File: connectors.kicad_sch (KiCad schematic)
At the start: 5 parts

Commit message: Connect sensors to the MCU
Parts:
- gave numbers to parts that had none: 5
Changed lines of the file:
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@@
 (kicad_sch (version 20211123) (generator eeschema)
   (paper "A4")
+  (title_block
+    (date "2022-12-16")
+    (rev "0.1.0")
+  )
   (wire (pts (xy 219.71 95.25) (xy 220.98 95.25))
     (stroke (width 0) (type default) (color 0 0 0 0))
@@
   (symbol (lib_id "Connector_Generic:Conn_01x03") (at 226.06 97.79 0) (unit 1)
     (in_bom yes) (on_board yes)
-    (property "Reference" "J?" (id 0) (at 227.33 91.4401 0)
+    (property "Reference" "J7" (id 0) (at 227.33 91.4401 0)
       (effects (font (size 1.27 1.27)) (justify right))
     )
@@
   (symbol (lib_id "power:GND") (at 219.71 101.6 0) (unit 1)
     (in_bom yes) (on_board yes) (fields_autoplaced)
-    (property "Reference" "#PWR?" (id 0) (at 219.71 107.95 0)
+    (property "Reference" "#PWR0145" (id 0) (at 219.71 107.95 0)
       (effects (font (size 1.27 1.27)) hide)
     )
@@
   (symbol (lib_id "Connector_Generic:Conn_01x03") (at 190.5 97.79 0) (unit 1)
     (in_bom yes) (on_board yes)
-    (property "Reference" "J?" (id 0) (at 191.77 91.4401 0)
+    (property "Reference" "J6" (id 0) (at 191.77 91.4401 0)
       (effects (font (size 1.27 1.27)) (justify right))
     )
@@
   (symbol (lib_id "power:GND") (at 114.3 101.6 0) (unit 1)
     (in_bom yes) (on_board yes) (fields_autoplaced)
-    (property "Reference" "#PWR?" (id 0) (at 114.3 107.95 0)
+    (property "Reference" "#PWR0143" (id 0) (at 114.3 107.95 0)
       (effects (font (size 1.27 1.27)) hide)
     )
@@
   (symbol (lib_id "power:+3.3V") (at 184.15 93.98 0) (unit 1)
     (in_bom yes) (on_board yes) (fields_autoplaced)
-    (property "Reference" "#PWR?" (id 0) (at 184.15 97.79 0)
+    (property "Reference" "#PWR0146" (id 0) (at 184.15 97.79 0)
       (effects (font (size 1.27 1.27)) hide)
     )
@@
   (symbol (lib_id "power:GND") (at 148.59 101.6 0) (unit 1)
     (in_bom yes) (on_board yes) (fields_autoplaced)
-    (property "Reference" "#PWR?" (id 0) (at 148.59 107.95 0)
+    (property "Reference" "#PWR0141" (id 0) (at 148.59 107.95 0)
       (effects (font (size 1.27 1.27)) hide)
     )
@@
   (symbol (lib_id "power:GND") (at 184.15 101.6 0) (unit 1)
     (in_bom yes) (on_board yes) (fields_autoplaced)
-    (property "Reference" "#PWR?" (id 0) (at 184.15 107.95 0)
+    (property "Reference" "#PWR0147" (id 0) (at 184.15 107.95 0)
       (effects (font (size 1.27 1.27)) hide)
     )
@@
   (symbol (lib_id "power:+3.3V") (at 219.71 93.98 0) (unit 1)
     (in_bom yes) (on_board yes) (fields_autoplaced)
-    (property "Reference" "#PWR?" (id 0) (at 219.71 97.79 0)
+    (property "Reference" "#PWR0144" (id 0) (at 219.71 97.79 0)
       (effects (font (size 1.27 1.27)) hide)
     )
@@
   (symbol (lib_id "power:GND") (at 86.36 101.6 0) (unit 1)
     (in_bom yes) (on_board yes) (fields_autoplaced)
-    (property "Reference" "#PWR?" (id 0) (at 86.36 107.95 0)
+    (property "Reference" "#PWR0138" (id 0) (at 86.36 107.95 0)
       (effects (font (size 1.27 1.27)) hide)
     )
@@
   (symbol (lib_id "Connector_Generic:Conn_01x03") (at 120.65 97.79 0) (unit 1)
     (in_bom yes) (on_board yes)
-    (property "Reference" "J?" (id 0) (at 119.38 91.4399 0)
+    (property "Reference" "J4" (id 0) (at 119.38 91.4399 0)
       (effects (font (size 1.27 1.27)) (justify left))
     )
@@
   (symbol (lib_id "power:VCC") (at 86.36 93.98 0) (unit 1)
     (in_bom yes) (on_board yes) (fields_autoplaced)
-    (property "Reference" "#PWR?" (id 0) (at 86.36 97.79 0)
+    (property "Reference" "#PWR0139" (id 0) (at 86.36 97.79 0)
       (effects (font (size 1.27 1.27)) hide)
     )
@@
   (symbol (lib_id "power:+5V") (at 114.3 93.98 0) (unit 1)
     (in_bom yes) (on_board yes) (fields_autoplaced)
-    (property "Reference" "#PWR?" (id 0) (at 114.3 97.79 0)
+    (property "Reference" "#PWR0142" (id 0) (at 114.3 97.79 0)
       (effects (font (size 1.27 1.27)) hide)
     )
@@
   (symbol (lib_id "power:+5V") (at 148.59 93.98 0) (unit 1)
     (in_bom yes) (on_board yes) (fields_autoplaced)
-    (property "Reference" "#PWR?" (id 0) (at 148.59 97.79 0)
+    (property "Reference" "#PWR0140" (id 0) (at 148.59 97.79 0)
       (effects (font (size 1.27 1.27)) hide)
     )
@@
   (symbol (lib_id "Connector_Generic:Conn_01x02") (at 78.74 96.52 0) (mirror y) (unit 1)
     (in_bom yes) (on_board yes)
-    (property "Reference" "J?" (id 0) (at 78.74 92.71 0))
+    (property "Reference" "J3" (id 0) (at 78.74 92.71 0))
     (property "Value" "Battery Pack" (id 1) (at 82.55 85.09 0))
     (property "Footprint" "" (id 2) (at 78.74 96.52 0)
@@
   (symbol (lib_id "Connector_Generic:Conn_01x03") (at 154.94 97.79 0) (unit 1)
     (in_bom yes) (on_board yes)
-    (property "Reference" "J?" (id 0) (at 153.67 91.4399 0)
+    (property "Reference" "J5" (id 0) (at 153.67 91.4399 0)
       (effects (font (size 1.27 1.27)) (justify left))
     )

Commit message: Improve the power section:
- add ADC circuit to measure battery level
- add 5V LDO regulator
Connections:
- net +3.3V is gone; now on net +5V: J6.1 (Pin_1), J7.1 (Pin_1)
- net VCC renamed +BATT
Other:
- moved on the sheet: J3
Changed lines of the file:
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@@
   (paper "A4")
   (title_block
-    (date "2022-12-16")
+    (date "2022-12-17")
     (rev "0.1.0")
   )
@@
     (stroke (width 0) (type default) (color 0 0 0 0))
   )
-  (wire (pts (xy 83.82 96.52) (xy 86.36 96.52))
+  (wire (pts (xy 85.09 96.52) (xy 86.36 96.52))
     (stroke (width 0) (type default) (color 0 0 0 0))
   )
@@
     (stroke (width 0) (type default) (color 0 0 0 0))
   )
-  (wire (pts (xy 83.82 99.06) (xy 86.36 99.06))
+  (wire (pts (xy 85.09 99.06) (xy 86.36 99.06))
     (stroke (width 0) (type default) (color 0 0 0 0))
   )
@@
   (symbol (lib_id "power:GND") (at 219.71 101.6 0) (unit 1)
     (in_bom yes) (on_board yes) (fields_autoplaced)
-    (property "Reference" "#PWR0145" (id 0) (at 219.71 107.95 0)
+    (property "Reference" "#PWR052" (id 0) (at 219.71 107.95 0)
       (effects (font (size 1.27 1.27)) hide)
     )
@@
   (symbol (lib_id "power:GND") (at 114.3 101.6 0) (unit 1)
     (in_bom yes) (on_board yes) (fields_autoplaced)
-    (property "Reference" "#PWR0143" (id 0) (at 114.3 107.95 0)
+    (property "Reference" "#PWR049" (id 0) (at 114.3 107.95 0)
       (effects (font (size 1.27 1.27)) hide)
     )
@@
     (pin "1")
   )
-  (symbol (lib_id "power:+3.3V") (at 184.15 93.98 0) (unit 1)
-    (in_bom yes) (on_board yes) (fields_autoplaced)
-    (property "Reference" "#PWR0146" (id 0) (at 184.15 97.79 0)
-      (effects (font (size 1.27 1.27)) hide)
-    )
-    (property "Value" "+3.3V" (id 1) (at 184.15 88.9 0))
-    (property "Footprint" "" (id 2) (at 184.15 93.98 0)
-      (effects (font (size 1.27 1.27)) hide)
-    )
-    (property "Datasheet" "" (id 3) (at 184.15 93.98 0)
+  (symbol (lib_id "power:+5V") (at 219.71 93.98 0) (unit 1)
+    (in_bom yes) (on_board yes) (fields_autoplaced)
+    (property "Reference" "#PWR047" (id 0) (at 219.71 97.79 0)
+      (effects (font (size 1.27 1.27)) hide)
+    )
+    (property "Value" "+5V" (id 1) (at 219.71 88.9 0))
+    (property "Footprint" "" (id 2) (at 219.71 93.98 0)
+      (effects (font (size 1.27 1.27)) hide)
+    )
+    (property "Datasheet" "" (id 3) (at 219.71 93.98 0)
       (effects (font (size 1.27 1.27)) hide)
     )
@@
   (symbol (lib_id "power:GND") (at 148.59 101.6 0) (unit 1)
     (in_bom yes) (on_board yes) (fields_autoplaced)
-    (property "Reference" "#PWR0141" (id 0) (at 148.59 107.95 0)
+    (property "Reference" "#PWR050" (id 0) (at 148.59 107.95 0)
       (effects (font (size 1.27 1.27)) hide)
     )
@@
   (symbol (lib_id "power:GND") (at 184.15 101.6 0) (unit 1)
     (in_bom yes) (on_board yes) (fields_autoplaced)
-    (property "Reference" "#PWR0147" (id 0) (at 184.15 107.95 0)
+    (property "Reference" "#PWR051" (id 0) (at 184.15 107.95 0)
       (effects (font (size 1.27 1.27)) hide)
     )
@@
     (pin "1")
   )
-  (symbol (lib_id "power:+3.3V") (at 219.71 93.98 0) (unit 1)
-    (in_bom yes) (on_board yes) (fields_autoplaced)
-    (property "Reference" "#PWR0144" (id 0) (at 219.71 97.79 0)
-      (effects (font (size 1.27 1.27)) hide)
-    )
-    (property "Value" "+3.3V" (id 1) (at 219.71 88.9 0))
-    (property "Footprint" "" (id 2) (at 219.71 93.98 0)
-      (effects (font (size 1.27 1.27)) hide)
-    )
-    (property "Datasheet" "" (id 3) (at 219.71 93.98 0)
+  (symbol (lib_id "power:+5V") (at 184.15 93.98 0) (unit 1)
+    (in_bom yes) (on_board yes) (fields_autoplaced)
+    (property "Reference" "#PWR046" (id 0) (at 184.15 97.79 0)
+      (effects (font (size 1.27 1.27)) hide)
+    )
+    (property "Value" "+5V" (id 1) (at 184.15 88.9 0))
+    (property "Footprint" "" (id 2) (at 184.15 93.98 0)
+      (effects (font (size 1.27 1.27)) hide)
+    )
+    (property "Datasheet" "" (id 3) (at 184.15 93.98 0)
       (effects (font (size 1.27 1.27)) hide)
     )
@@
   (symbol (lib_id "power:GND") (at 86.36 101.6 0) (unit 1)
     (in_bom yes) (on_board yes) (fields_autoplaced)
-    (property "Reference" "#PWR0138" (id 0) (at 86.36 107.95 0)
+    (property "Reference" "#PWR048" (id 0) (at 86.36 107.95 0)
       (effects (font (size 1.27 1.27)) hide)
     )
@@
     (pin "3")
   )
-  (symbol (lib_id "power:VCC") (at 86.36 93.98 0) (unit 1)
-    (in_bom yes) (on_board yes) (fields_autoplaced)
-    (property "Reference" "#PWR0139" (id 0) (at 86.36 97.79 0)
-      (effects (font (size 1.27 1.27)) hide)
-    )
-    (property "Value" "VCC" (id 1) (at 86.36 88.9 0))
-    (property "Footprint" "" (id 2) (at 86.36 93.98 0)
-      (effects (font (size 1.27 1.27)) hide)
-    )
-    (property "Datasheet" "" (id 3) (at 86.36 93.98 0)
-      (effects (font (size 1.27 1.27)) hide)
-    )
-    (pin "1")
-  )
   (symbol (lib_id "power:+5V") (at 114.3 93.98 0) (unit 1)
     (in_bom yes) (on_board yes) (fields_autoplaced)
-    (property "Reference" "#PWR0142" (id 0) (at 114.3 97.79 0)
+    (property "Reference" "#PWR044" (id 0) (at 114.3 97.79 0)
       (effects (font (size 1.27 1.27)) hide)
     )
@@
     (pin "1")
   )
+  (symbol (lib_id "power:+BATT") (at 86.36 93.98 0) (unit 1)
+    (in_bom yes) (on_board yes) (fields_autoplaced)
+    (property "Reference" "#PWR043" (id 0) (at 86.36 97.79 0)
+      (effects (font (size 1.27 1.27)) hide)
+    )
+    (property "Value" "+BATT" (id 1) (at 86.36 88.9 0))
+    (property "Footprint" "" (id 2) (at 86.36 93.98 0)
+      (effects (font (size 1.27 1.27)) hide)
+    )
+    (property "Datasheet" "" (id 3) (at 86.36 93.98 0)
+      (effects (font (size 1.27 1.27)) hide)
+    )
+    (pin "1")
+  )
   (symbol (lib_id "power:+5V") (at 148.59 93.98 0) (unit 1)
     (in_bom yes) (on_board yes) (fields_autoplaced)
-    (property "Reference" "#PWR0140" (id 0) (at 148.59 97.79 0)
+    (property "Reference" "#PWR045" (id 0) (at 148.59 97.79 0)
       (effects (font (size 1.27 1.27)) hide)
     )
@@
     (pin "1")
   )
-  (symbol (lib_id "Connector_Generic:Conn_01x02") (at 78.74 96.52 0) (mirror y) (unit 1)
+  (symbol (lib_id "Connector_Generic:Conn_01x02") (at 80.01 96.52 0) (mirror y) (unit 1)
     (in_bom yes) (on_board yes)
-    (property "Reference" "J3" (id 0) (at 78.74 92.71 0))
-    (property "Value" "Battery Pack" (id 1) (at 82.55 85.09 0))
-    (property "Footprint" "" (id 2) (at 78.74 96.52 0)
-      (effects (font (size 1.27 1.27)) hide)
-    )
-    (property "Datasheet" "~" (id 3) (at 78.74 96.52 0)
-      (effects (font (size 1.27 1.27)) hide)
-    )
+    (property "Reference" "J3" (id 0) (at 80.01 92.71 0))
+    (property "Value" "Battery Pack" (id 1) (at 83.82 85.09 0))
+    (property "Footprint" "" (id 2) (at 80.01 96.52 0)
+      (effects (font (size 1.27 1.27)) hide)
+    )
+    (property "Datasheet" "~" (id 3) (at 80.01 96.52 0)
+      (effects (font (size 1.27 1.27)) hide)
+    )

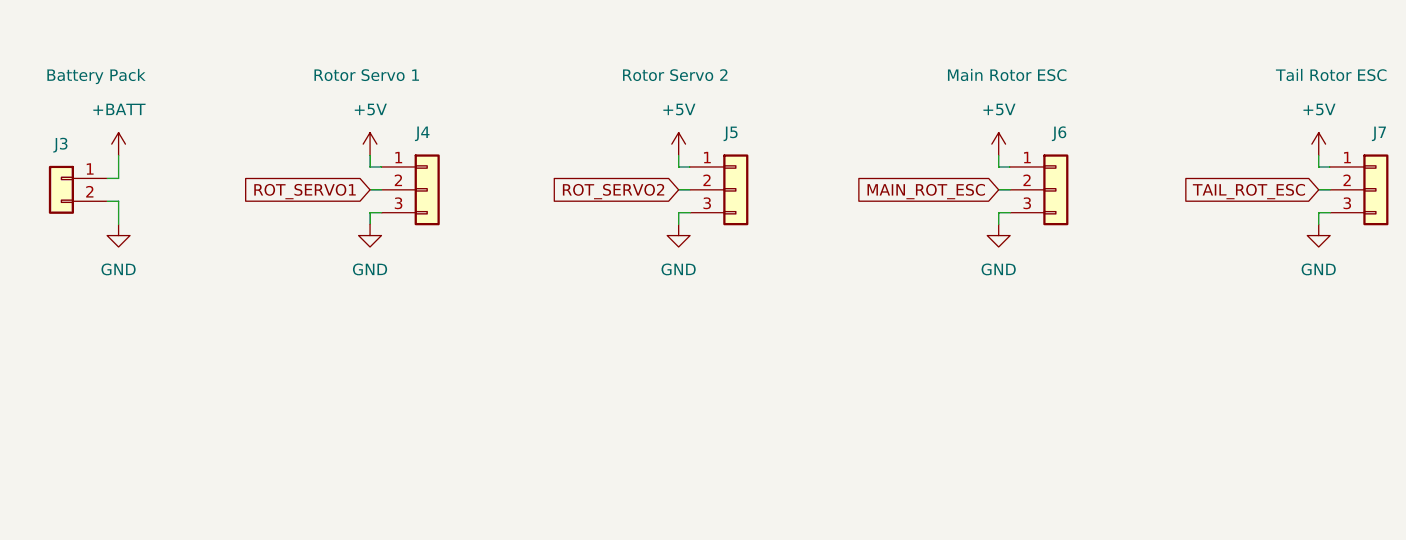
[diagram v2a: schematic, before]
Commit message: Add external UART and I2C connectors
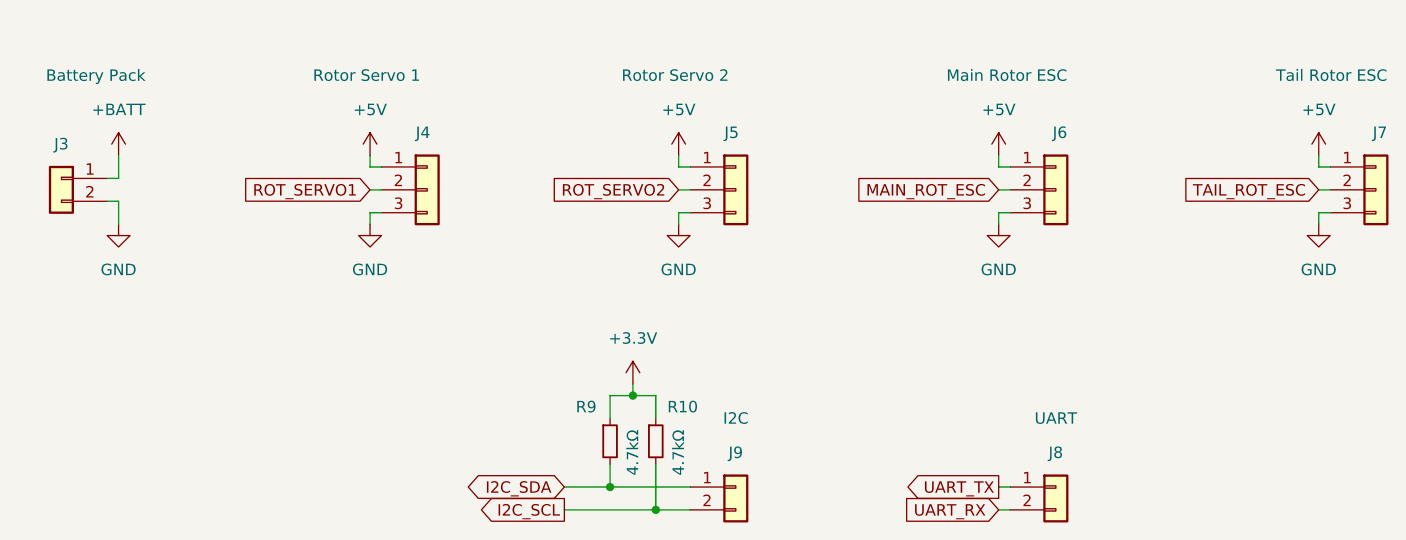
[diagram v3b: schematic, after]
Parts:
- added J8: UART, symbol Connector_Generic:Conn_01x02
- added J9: I2C, symbol Connector_Generic:Conn_01x02
- added R10, R9: 4.7kΩ, Resistor_SMD:R_0603_1608Metric, symbol Device:R_Small
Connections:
- new net +3.3V: R10.1, R9.1
- new net I2C_SCL: J9.2 (Pin_2), R10.2
- new net I2C_SDA: J9.1 (Pin_1), R9.2
- new net UART_RX: J8.2 (Pin_2)
- new net UART_TX: J8.1 (Pin_1)
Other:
- title: (none) -> Connectors
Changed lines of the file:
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@@
   (paper "A4")
   (title_block
+    (title "Connectors")
     (date "2022-12-17")
     (rev "0.1.0")
   )
+  (junction (at 146.05 133.35) (diameter 0) (color 0 0 0 0)
+  )
+  (junction (at 143.51 120.65) (diameter 0) (color 0 0 0 0)
+  )
+  (junction (at 140.97 130.81) (diameter 0) (color 0 0 0 0)
+  )
   (wire (pts (xy 219.71 95.25) (xy 220.98 95.25))
     (stroke (width 0) (type default) (color 0 0 0 0))
@@
     (stroke (width 0) (type default) (color 0 0 0 0))
   )
+  (wire (pts (xy 185.42 133.35) (xy 184.15 133.35))
+    (stroke (width 0) (type default) (color 0 0 0 0))
+  )
+  (wire (pts (xy 146.05 120.65) (xy 143.51 120.65))
+    (stroke (width 0) (type default) (color 0 0 0 0))
+  )
+  (wire (pts (xy 146.05 123.19) (xy 146.05 120.65))
+    (stroke (width 0) (type default) (color 0 0 0 0))
+  )
   (wire (pts (xy 219.71 100.33) (xy 220.98 100.33))
     (stroke (width 0) (type default) (color 0 0 0 0))
   )
+  (wire (pts (xy 143.51 120.65) (xy 140.97 120.65))
+    (stroke (width 0) (type default) (color 0 0 0 0))
+  )
   (wire (pts (xy 219.71 97.79) (xy 220.98 97.79))
     (stroke (width 0) (type default) (color 0 0 0 0))
@@
     (stroke (width 0) (type default) (color 0 0 0 0))
   )
+  (wire (pts (xy 140.97 120.65) (xy 140.97 123.19))
+    (stroke (width 0) (type default) (color 0 0 0 0))
+  )
+  (wire (pts (xy 146.05 128.27) (xy 146.05 133.35))
+    (stroke (width 0) (type default) (color 0 0 0 0))
+  )
+  (wire (pts (xy 185.42 130.81) (xy 184.15 130.81))
+    (stroke (width 0) (type default) (color 0 0 0 0))
+  )
+  (wire (pts (xy 143.51 119.38) (xy 143.51 120.65))
+    (stroke (width 0) (type default) (color 0 0 0 0))
+  )
   (wire (pts (xy 148.59 93.98) (xy 148.59 95.25))
     (stroke (width 0) (type default) (color 0 0 0 0))
@@
     (stroke (width 0) (type default) (color 0 0 0 0))
   )
+  (wire (pts (xy 140.97 130.81) (xy 149.86 130.81))
+    (stroke (width 0) (type default) (color 0 0 0 0))
+  )
+  (wire (pts (xy 146.05 133.35) (xy 149.86 133.35))
+    (stroke (width 0) (type default) (color 0 0 0 0))
+  )
   (wire (pts (xy 85.09 99.06) (xy 86.36 99.06))
     (stroke (width 0) (type default) (color 0 0 0 0))
@@
     (stroke (width 0) (type default) (color 0 0 0 0))
   )
+  (wire (pts (xy 140.97 128.27) (xy 140.97 130.81))
+    (stroke (width 0) (type default) (color 0 0 0 0))
+  )
   (wire (pts (xy 148.59 97.79) (xy 149.86 97.79))
     (stroke (width 0) (type default) (color 0 0 0 0))
   )
+  (wire (pts (xy 135.89 130.81) (xy 140.97 130.81))
+    (stroke (width 0) (type default) (color 0 0 0 0))
+  )
   (wire (pts (xy 184.15 93.98) (xy 184.15 95.25))
     (stroke (width 0) (type default) (color 0 0 0 0))
@@
     (stroke (width 0) (type default) (color 0 0 0 0))
   )
+  (wire (pts (xy 135.89 133.35) (xy 146.05 133.35))
+    (stroke (width 0) (type default) (color 0 0 0 0))
+  )
+  (global_label "I2C_SCL" (shape output) (at 135.89 133.35 180) (fields_autoplaced)
+    (effects (font (size 1.27 1.27)) (justify right))
+    (property "Intersheet References" "${INTERSHEET_REFS}" (id 0) (at 125.9174 133.2706 0)
+      (effects (font (size 1.27 1.27)) (justify right) hide)
+    )
+  )
   (global_label "ROT_SERVO2" (shape input) (at 148.59 97.79 180) (fields_autoplaced)
     (effects (font (size 1.27 1.27)) (justify right))
@@
     )
   )
+  (global_label "I2C_SDA" (shape bidirectional) (at 135.89 130.81 180) (fields_autoplaced)
+    (effects (font (size 1.27 1.27)) (justify right))
+    (property "Intersheet References" "${INTERSHEET_REFS}" (id 0) (at 125.8569 130.7306 0)
+      (effects (font (size 1.27 1.27)) (justify right) hide)
+    )
+  )
   (global_label "TAIL_ROT_ESC" (shape input) (at 219.71 97.79 180) (fields_autoplaced)
     (effects (font (size 1.27 1.27)) (justify right))
     (property "Intersheet References" "${INTERSHEET_REFS}" (id 0) (at 204.4759 97.7106 0)
+      (effects (font (size 1.27 1.27)) (justify right) hide)
+    )
+  )
+  (global_label "UART_TX" (shape output) (at 184.15 130.81 180) (fields_autoplaced)
+    (effects (font (size 1.27 1.27)) (justify right))
+    (property "Intersheet References" "${INTERSHEET_REFS}" (id 0) (at 173.9355 130.7306 0)
+      (effects (font (size 1.27 1.27)) (justify right) hide)
+    )
+  )
+  (global_label "UART_RX" (shape input) (at 184.15 133.35 180) (fields_autoplaced)
+    (effects (font (size 1.27 1.27)) (justify right))
+    (property "Intersheet References" "${INTERSHEET_REFS}" (id 0) (at 173.6331 133.2706 0)
       (effects (font (size 1.27 1.27)) (justify right) hide)
     )
@@
     (pin "1")
   )
+  (symbol (lib_id "Connector_Generic:Conn_01x02") (at 154.94 130.81 0) (unit 1)
+    (in_bom yes) (on_board yes)
+    (property "Reference" "J9" (id 0) (at 154.94 127 0))
+    (property "Value" "I2C" (id 1) (at 154.94 123.19 0))
+    (property "Footprint" "" (id 2) (at 154.94 130.81 0)
+      (effects (font (size 1.27 1.27)) hide)
+    )
+    (property "Datasheet" "~" (id 3) (at 154.94 130.81 0)
+      (effects (font (size 1.27 1.27)) hide)
+    )
+    (pin "1")
+    (pin "2")
+  )
   (symbol (lib_id "power:GND") (at 86.36 101.6 0) (unit 1)
     (in_bom yes) (on_board yes) (fields_autoplaced)
@@
     )
     (pin "1")
+  )
+  (symbol (lib_id "Device:R_Small") (at 140.97 125.73 0) (unit 1)
+    (in_bom yes) (on_board yes)
+    (property "Reference" "R9" (id 0) (at 137.16 121.9199 0)
+      (effects (font (size 1.27 1.27)) (justify left))
+    )
+    (property "Value" "4.7kΩ" (id 1) (at 143.51 129.5399 90)
+      (effects (font (size 1.27 1.27)) (justify left))
+    )
+    (property "Footprint" "Resistor_SMD:R_0603_1608Metric" (id 2) (at 140.97 125.73 0)
+      (effects (font (size 1.27 1.27)) hide)
+    )
+    (property "Datasheet" "~" (id 3) (at 140.97 125.73 0)
+      (effects (font (size 1.27 1.27)) hide)
+    )
+    (pin "1")
+    (pin "2")
+  )
+  (symbol (lib_id "Device:R_Small") (at 146.05 125.73 0) (unit 1)
+    (in_bom yes) (on_board yes)
+    (property "Reference" "R10" (id 0) (at 147.32 121.9199 0)
+      (effects (font (size 1.27 1.27)) (justify left))
+    )
+    (property "Value" "4.7kΩ" (id 1) (at 148.59 129.5399 90)
+      (effects (font (size 1.27 1.27)) (justify left))
+    )
+    (property "Footprint" "Resistor_SMD:R_0603_1608Metric" (id 2) (at 146.05 125.73 0)
+      (effects (font (size 1.27 1.27)) hide)
+    )
+    (property "Datasheet" "~" (id 3) (at 146.05 125.73 0)
+      (effects (font (size 1.27 1.27)) hide)
+    )
+    (pin "1")
+    (pin "2")
   )
   (symbol (lib_id "power:+BATT") (at 86.36 93.98 0) (unit 1)
@@
       (effects (font (size 1.27 1.27)) hide)
     )
+    (pin "1")
+    (pin "2")
+  )
+  (symbol (lib_id "power:+3.3V") (at 143.51 119.38 0) (unit 1)
+    (in_bom yes) (on_board yes)
+    (property "Reference" "#PWR053" (id 0) (at 143.51 123.19 0)
+      (effects (font (size 1.27 1.27)) hide)
+    )
+    (property "Value" "+3.3V" (id 1) (at 143.51 114.3 0))
+    (property "Footprint" "" (id 2) (at 143.51 119.38 0)
+      (effects (font (size 1.27 1.27)) hide)
+    )
+    (property "Datasheet" "" (id 3) (at 143.51 119.38 0)
+      (effects (font (size 1.27 1.27)) hide)
+    )
+    (pin "1")
+  )
+  (symbol (lib_id "Connector_Generic:Conn_01x02") (at 190.5 130.81 0) (unit 1)
+    (in_bom yes) (on_board yes)
+    (property "Reference" "J8" (id 0) (at 190.5 127 0))
+    (property "Value" "UART" (id 1) (at 190.5 123.19 0))
+    (property "Footprint" "" (id 2) (at 190.5 130.81 0)
+      (effects (font (size 1.27 1.27)) hide)
+    )
+    (property "Datasheet" "~" (id 3) (at 190.5 130.81 0)
+      (effects (font (size 1.27 1.27)) hide)
+    )
